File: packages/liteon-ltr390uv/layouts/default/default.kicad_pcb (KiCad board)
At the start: 2 copper layers, 5 parts

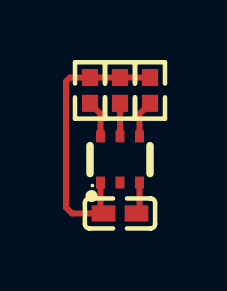
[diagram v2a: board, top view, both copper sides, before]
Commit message: Upgrade Packages: Narayans Half (#185)
* adi-ad5693r

* fix frozen

* prjc-teensy_4_1

* rp2040

* adi-adxl375: Add missing usage build target to ato.yaml

* adi-ds2482s-800: Update layout files after build

* adi-ltc4311: Update layout to fix frozen build

- Updated net names (BUS1/BUS2 → SDA/SCL, gnd → GND, hv → VCC)
- Fixed footprint properties and coordinates
- Package now passes frozen build and verification

* awinic-aw9523: Update layout to fix frozen build

- Updated net names (AD0/AD1 → address_bit_0/address_bit_1, hv → VCC, gnd → GND)
- Updated GPIO line names (-line-0 → gpios[8]-line, etc.)
- Fixed footprint properties and coordinates
- Package now passes frozen build and verification

* awinic-aw9523: Bump version to 0.1.1

- Version bump due to layout updates to fix frozen build

* adi-adbms6830: Fix package verify issues

- Add has_part_removed trait to components missing pickers (atopile_logo, SPDT, analog_DPDT)
- Add missing import for has_part_removed trait
- Add exclude_checks to usage build in ato.yaml
- Update README.md to match usage.ato content
- Bump version from 0.1.2 to 0.1.3

Package now passes ato package verify -s

* indicator-leds: Update layout and bump version

- Updated PCB layout coordinates to fix frozen build issues
- Bumped version from 0.1.5 to 0.1.6
- Package now passes ato package verify -s successfully

* Bump package versions for done packages

- adi-adxl345: 0.1.1 -> 0.1.2
- adi-adxl375: 0.1.0 -> 0.1.1
- adi-ds2482s-800: 0.1.0 -> 0.1.1
- adi-ltc4311: 0.1.0 -> 0.1.1
- adi-ltc4316: 0.1.0 -> 0.1.1
- ams-tsl2591: 0.1.0 -> 0.1.1

These packages were marked as 'Done' in package-todos.md but had version
warnings during package verification. Version bumps ensure they can be
published to the registry.

* invensense-mpu6050: Update layout files and bump version to 0.1.2

* Fix picker warnings by adding has_part_removed trait to MCU modules

- Added #pragma experiment("TRAITS") to enable traits feature
- Added import has_part_removed t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
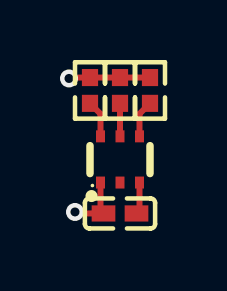
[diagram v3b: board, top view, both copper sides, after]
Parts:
- R2, R3: value 10kΩ ±1% 62.5mW -> 4.7kΩ ±1% 62.5mW; footprint UNI_ROYAL_0402WGF1002TCE:R0402 -> UNI_ROYAL_0402WGF4701TCE:R0402
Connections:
- net VDD renamed VCC
- net gnd renamed GND
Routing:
- net VCC: track 9.46 -> 4.75 mm, vias 0 -> 2

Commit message: liteon-ltr390uv: package update to v0.2.0, ato:^0.14.0
Build targets:
  default = rc0
  usage = rc0
Package Verify: rc0
Version: 0.1.1 -> 0.2.0
Requires ato: ^0.14.0
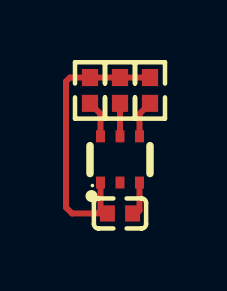
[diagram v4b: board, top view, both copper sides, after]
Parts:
- C1: value 100nF ±10% 16V X7R -> 1F
- R1: value 10kΩ ±1% 62.5mW -> 10000Ω
- R2, R3: value 4.7kΩ ±1% 62.5mW -> 4700Ω
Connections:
- net GND renamed lv
- net VCC renamed hv
- U1 pad 2: net -> (no net)
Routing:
- net 4: track 0.00 -> 9.46 mm
- net hv: track 4.75 -> 0.00 mm, vias 2 -> 0
- net lv: track 1.07 -> 0.00 mm
- net 1: track 0.00 -> 1.07 mm
